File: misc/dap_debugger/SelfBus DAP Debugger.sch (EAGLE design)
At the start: 60 parts, among them CON1 MICRO-B_U254-051N-4BH806, CON2 SHF-105-01-X-D-TH, CON3 SHF-105-01-X-D-TH, CON4 SAMTEC-LTMM-105-02-T-D, IC1 74LVC1T45GW, IC2 74LVC2G07GV, IC3 74LVC2T45DC, IC4 74LVC2T45DC, SW1 BOOT, SW2 RESET, SW3 XKB7070-Z, U1 STM32F042FX, U2 AP2112K-3.3TRG1, U3 AP2331TDW

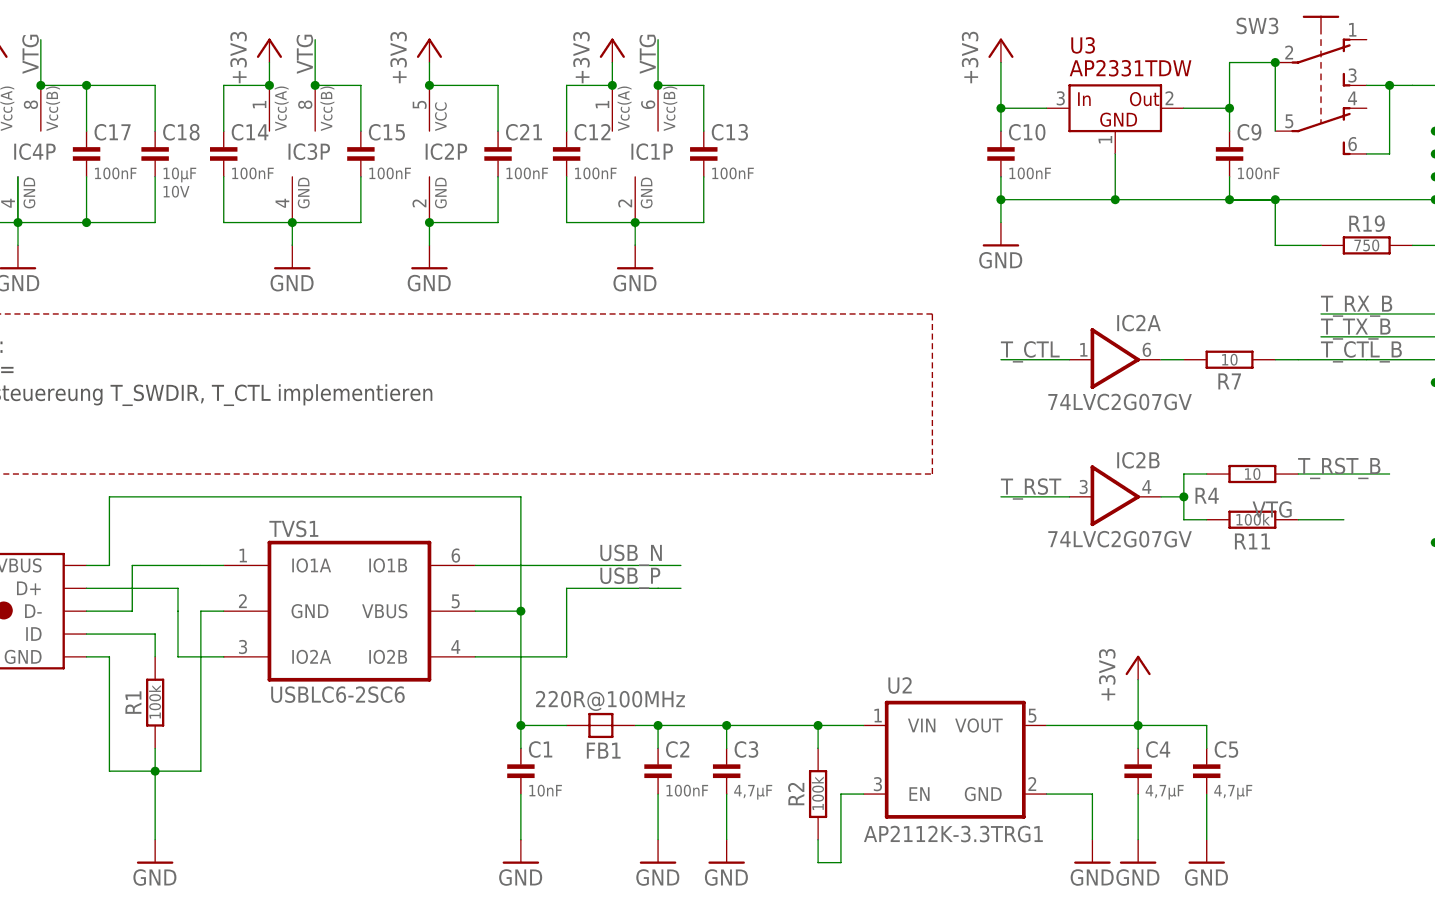
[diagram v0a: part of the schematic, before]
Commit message: [SB-DAP] - changed values to standard values
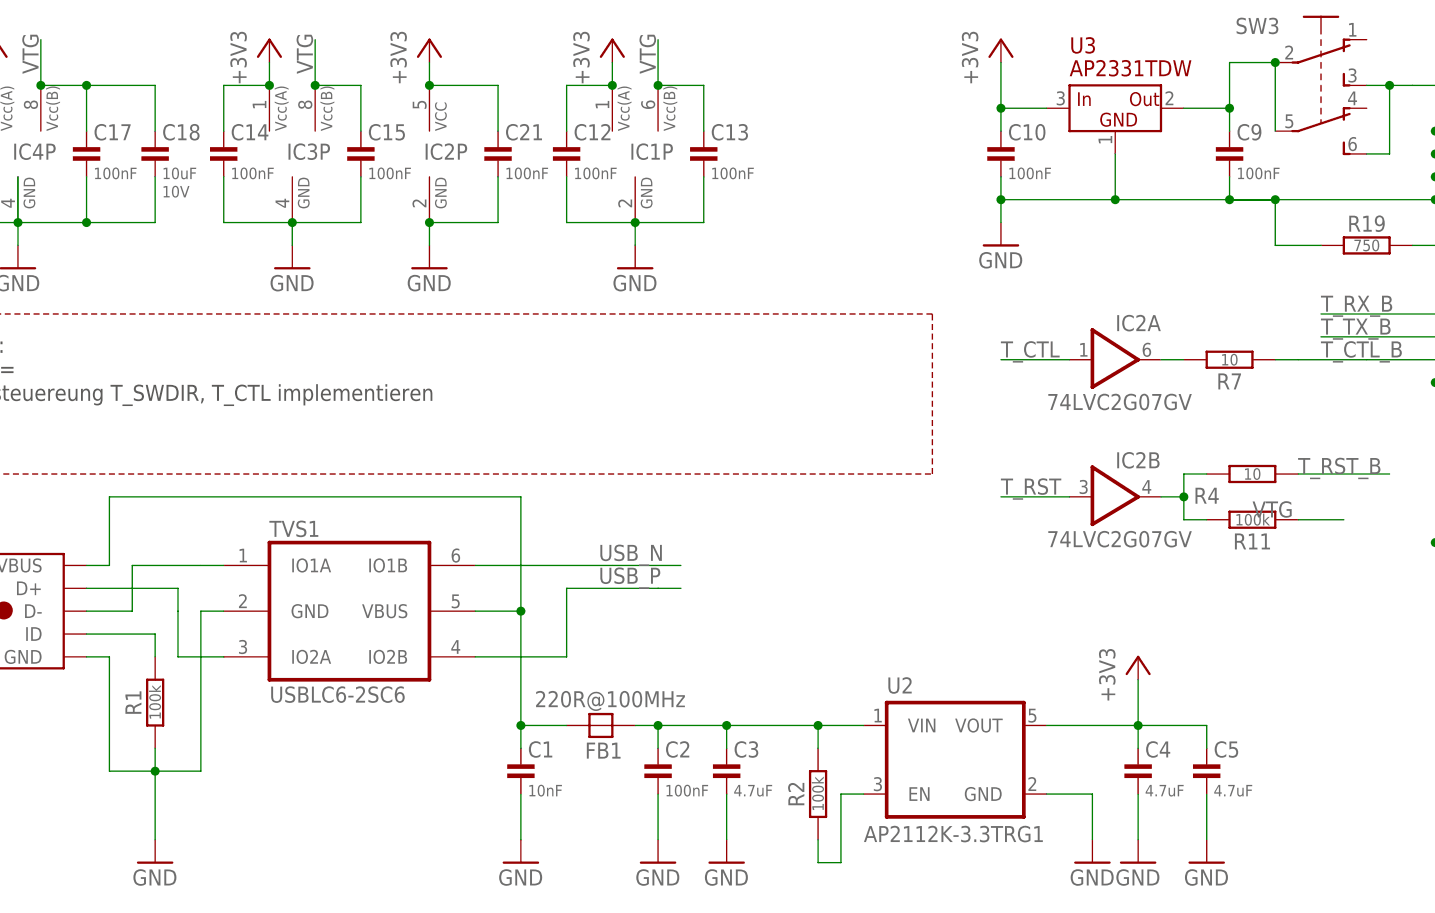
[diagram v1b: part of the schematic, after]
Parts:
- C18: value 10µF -> 10uF
- C3, C4, C5: value 4,7µF -> 4.7uF
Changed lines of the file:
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@@
 <drawing>
 <settings>
-<setting alwaysvectorfont="yes"/>
+<setting alwaysvectorfont="no"/>
 <setting verticaltext="up"/>
 </settings>
@@
 <part name="C1" library="MyRCL" deviceset="C-EU" device="C0805" package3d_urn="urn:adsk.eagle:package:23617/2" value="10nF"/>
 <part name="C2" library="MyRCL" deviceset="C-EU" device="C0805" package3d_urn="urn:adsk.eagle:package:23617/2" value="100nF"/>
-<part name="C3" library="MyRCL" deviceset="C-EU" device="C0805" package3d_urn="urn:adsk.eagle:package:23617/2" value="4,7µF"/>
+<part name="C3" library="MyRCL" deviceset="C-EU" device="C0805" package3d_urn="urn:adsk.eagle:package:23617/2" value="4.7uF"/>
 <part name="FB1" library="MyEMC-Components" deviceset="FB" device="" package3d_urn="urn:adsk.eagle:package:24756627/3" value="220R@100MHz">
 <attribute name="LCSC#2" value="C139188"/>
@@
 <part name="R2" library="MyRCL" deviceset="R-EU_" device="R0805" package3d_urn="urn:adsk.eagle:package:18594703/1" value="100k"/>
 <part name="GND6" library="supply1" library_urn="urn:adsk.eagle:library:371" deviceset="GND" device=""/>
-<part name="C4" library="MyRCL" deviceset="C-EU" device="C0805" package3d_urn="urn:adsk.eagle:package:23617/2" value="4,7µF"/>
+<part name="C4" library="MyRCL" deviceset="C-EU" device="C0805" package3d_urn="urn:adsk.eagle:package:23617/2" value="4.7uF"/>
 <part name="GND7" library="supply1" library_urn="urn:adsk.eagle:library:371" deviceset="GND" device=""/>
 <part name="+3V1" library="supply1" library_urn="urn:adsk.eagle:library:371" deviceset="+3V3" device=""/>
@@
 <attribute name="PART_MFR" value="ALPS"/>
 </part>
-<part name="C5" library="MyRCL" deviceset="C-EU" device="C0805" package3d_urn="urn:adsk.eagle:package:23617/2" value="4,7µF"/>
+<part name="C5" library="MyRCL" deviceset="C-EU" device="C0805" package3d_urn="urn:adsk.eagle:package:23617/2" value="4.7uF"/>
 <part name="GND12" library="supply1" library_urn="urn:adsk.eagle:library:371" deviceset="GND" device=""/>
 <part name="LED1" library="SelfBus DAP Debugger" library_urn="urn:adsk.eagle:library:29255033" deviceset="LED_3MM(T1)_YELLOW" device="" package3d_urn="urn:adsk.eagle:package:29257046/2" value="Run"/>
@@
 <part name="+3V11" library="supply1" library_urn="urn:adsk.eagle:library:371" deviceset="+3V3" device=""/>
 <part name="GND22" library="supply1" library_urn="urn:adsk.eagle:library:371" deviceset="GND" device=""/>
-<part name="C18" library="MyRCL" deviceset="C-EU" device="C0805" package3d_urn="urn:adsk.eagle:package:23617/2" value="10µF">
+<part name="C18" library="MyRCL" deviceset="C-EU" device="C0805" package3d_urn="urn:adsk.eagle:package:23617/2" value="10uF">
 <spice>
 <pinmapping spiceprefix="C">
